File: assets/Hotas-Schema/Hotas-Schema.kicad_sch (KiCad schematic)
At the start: 22 parts, among them SW1 SW_SPST, SW10 SW_SPST, SW2 SW_SPST, SW3 SW_SPST, SW4 SW_SPST, SW5 SW_SPST, SW6 SW_SPST, SW7 SW_SPST, SW8 SW_SPST, SW9 SW_SPST

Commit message: Finish the circuit schematic
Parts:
- Joystick1: symbol IoT:Joystick -> HumanInterface:Joystick
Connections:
- net at ProMicro1.14 (GND): now also Joystick1. (Y)
- net at ProMicro1.16 (VCC): now also Joystick1. (Y), RV1.1
- net at ProMicro1.17 (A3): now also RV1.2
- net at ProMicro1.19 (A1): now also Joystick1. (Y)
- net at ProMicro1.20 (A0): now also Joystick1. (Y)
- net at ProMicro1.21 (15): now also Joystick1. (Y)
- net at ProMicro1.22 (14): now also SW10.1 (A)
- net at ProMicro1.4 (GND): now also RV1.3, SW10.2 (B)
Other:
- note added: "04-03-2024"
- note added: "1.0"
- note added: "Lego Throttle joystick schematic"
- moved on the sheet: Joystick1, RV1, SW10
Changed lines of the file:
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@@
   (junction (at 117.856 104.14) (diameter 0) (color 0 0 0 0)
   )
+  (junction (at 135.89 83.312) (diameter 0) (color 0 0 0 0)
+  )
   (junction (at 107.696 111.76) (diameter 0) (color 0 0 0 0)
   )
   (junction (at 131.826 91.44) (diameter 0) (color 0 0 0 0)
   )
+  (junction (at 135.89 44.704) (diameter 0) (color 0 0 0 0)
+  )
   (junction (at 121.666 99.06) (diameter 0) (color 0 0 0 0)
   )
@@
   (junction (at 121.666 124.46) (diameter 0) (color 0 0 0 0)
   )
+  (wire (pts (xy 129.794 62.992) (xy 132.08 62.992))
+    (stroke (width 0) (type default))
+  )
+  (wire (pts (xy 143.764 57.404) (xy 143.764 67.056))
+    (stroke (width 0) (type default))
+  )
   (wire (pts (xy 145.796 84.328) (xy 145.796 91.44))
     (stroke (width 0) (type default))
   )
+  (wire (pts (xy 129.794 73.152) (xy 140.208 73.152))
+    (stroke (width 0) (type default))
+  )
+  (wire (pts (xy 151.638 71.12) (xy 129.794 71.12))
+    (stroke (width 0) (type default))
+  )
+  (wire (pts (xy 135.89 44.704) (xy 138.43 44.704))
+    (stroke (width 0) (type default))
+  )
   (wire (pts (xy 106.426 69.088) (xy 103.886 69.088))
     (stroke (width 0) (type default))
@@
     (stroke (width 0) (type default))
   )
+  (wire (pts (xy 151.638 57.404) (xy 151.638 71.12))
+    (stroke (width 0) (type default))
+  )
   (wire (pts (xy 101.854 111.76) (xy 107.696 111.76))
     (stroke (width 0) (type default))
   )
+  (wire (pts (xy 135.89 44.704) (xy 135.89 55.118))
+    (stroke (width 0) (type default))
+  )
+  (wire (pts (xy 135.89 83.312) (xy 140.208 83.312))
+    (stroke (width 0) (type default))
+  )
   (wire (pts (xy 103.886 86.36) (xy 117.856 86.36))
     (stroke (width 0) (type default))
@@
     (stroke (width 0) (type default))
   )
+  (wire (pts (xy 119.126 46.736) (xy 138.43 46.736))
+    (stroke (width 0) (type default))
+  )
   (wire (pts (xy 104.902 71.12) (xy 106.426 71.12))
     (stroke (width 0) (type default))
@@
     (stroke (width 0) (type default))
   )
+  (wire (pts (xy 147.828 57.404) (xy 147.828 69.088))
+    (stroke (width 0) (type default))
+  )
   (wire (pts (xy 131.826 91.44) (xy 131.826 104.14))
     (stroke (width 0) (type default))
   )
+  (wire (pts (xy 143.764 67.056) (xy 129.794 67.056))
+    (stroke (width 0) (type default))
+  )
   (wire (pts (xy 145.796 104.14) (xy 145.796 116.84))
     (stroke (width 0) (type default))
@@
     (stroke (width 0) (type default))
   )
+  (wire (pts (xy 135.89 62.738) (xy 135.89 83.312))
+    (stroke (width 0) (type default))
+  )
   (wire (pts (xy 131.826 91.44) (xy 131.826 85.344))
     (stroke (width 0) (type default))
@@
     (stroke (width 0) (type default))
   )
+  (wire (pts (xy 147.828 69.088) (xy 129.794 69.088))
+    (stroke (width 0) (type default))
+  )
+  (wire (pts (xy 117.094 44.704) (xy 135.89 44.704))
+    (stroke (width 0) (type default))
+  )
+  (wire (pts (xy 119.126 83.312) (xy 135.89 83.312))
+    (stroke (width 0) (type default))
+  )
   (wire (pts (xy 117.856 86.36) (xy 117.856 91.44))
     (stroke (width 0) (type default))
   )
+  (wire (pts (xy 119.126 83.312) (xy 119.126 82.804))
+    (stroke (width 0) (type default))
+  )
   (wire (pts (xy 104.902 85.344) (xy 104.902 71.12))
     (stroke (width 0) (type default))
@@
     (stroke (width 0) (type default))
   )
+  (wire (pts (xy 117.094 46.736) (xy 117.094 44.704))
+    (stroke (width 0) (type default))
+  )
   (wire (pts (xy 131.826 104.14) (xy 131.826 116.84))
     (stroke (width 0) (type default))
@@
   (wire (pts (xy 101.854 65.024) (xy 101.854 111.76))
     (stroke (width 0) (type default))
+  )
+  (wire (pts (xy 132.08 62.992) (xy 132.08 58.928))
+    (stroke (width 0) (type default))
+  )
+  (text "1.0" (at 267.97 194.31 0)
+    (effects (font (size 1.27 1.27) (thickness 0.254) bold) (justify left bottom))
+  )
+  (text "Lego Throttle joystick schematic" (at 185.166 191.262 0)
+    (effects (font (size 2.54 2.54) (thickness 0.508) bold italic) (justify left bottom))
+  )
+  (text "04-03-2024" (at 205.74 194.31 0)
+    (effects (font (size 1.27 1.27)) (justify left bottom))
   )
   (symbol (lib_id "Switch:SW_SPST") (at 140.716 91.44 0) (unit 1)
@@
     )
   )
-  (symbol (lib_id "IoT:Joystick") (at 154.94 49.53 270) (unit 1)
-    (in_bom yes) (on_board yes) (dnp no) (fields_autoplaced)
-    (property "Reference" "Joystick1" (at 162.56 49.403 90)
-      (effects (font (size 1.27 1.27)) (justify left))
-    )
-    (property "Value" "~" (at 154.94 49.53 0)
-      (effects (font (size 1.27 1.27)))
-    )
-    (property "Footprint" "" (at 154.94 49.53 0)
-      (effects (font (size 1.27 1.27)) hide)
-    )
-    (property "Datasheet" "" (at 154.94 49.53 0)
+  (symbol (lib_id "HumanInterface:Joystick") (at 147.828 48.768 0) (unit 1)
+    (in_bom yes) (on_board yes) (dnp no) (fields_autoplaced)
+    (property "Reference" "Joystick1" (at 155.448 48.768 0)
+      (effects (font (size 1.27 1.27)) (justify left))
+    )
+    (property "Value" "~" (at 147.828 48.768 0)
+      (effects (font (size 1.27 1.27)))
+    )
+    (property "Footprint" "" (at 147.828 48.768 0)
+      (effects (font (size 1.27 1.27)) hide)
+    )
+    (property "Datasheet" "" (at 147.828 48.768 0)
       (effects (font (size 1.27 1.27)) hide)
     )
@@
     )
   )
-  (symbol (lib_id "Device:R_Potentiometer") (at 158.75 62.23 270) (unit 1)
-    (in_bom yes) (on_board yes) (dnp no) (fields_autoplaced)
-    (property "Reference" "RV1" (at 158.75 58.42 90)
-      (effects (font (size 1.27 1.27)))
-    )
-    (property "Value" "R_Potentiometer" (at 158.75 58.42 90)
-      (effects (font (size 1.27 1.27)) hide)
-    )
-    (property "Footprint" "" (at 158.75 62.23 0)
-      (effects (font (size 1.27 1.27)) hide)
-    )
-    (property "Datasheet" "~" (at 158.75 62.23 0)
+  (symbol (lib_id "Device:R_Potentiometer") (at 135.89 58.928 0) (mirror y) (unit 1)
+    (in_bom yes) (on_board yes) (dnp no)
+    (property "Reference" "RV1" (at 138.43 58.928 0)
+      (effects (font (size 1.27 1.27)) (justify right))
+    )
+    (property "Value" "R_Potentiometer" (at 139.7 58.928 90)
+      (effects (font (size 1.27 1.27)) hide)
+    )
+    (property "Footprint" "" (at 135.89 58.928 0)
+      (effects (font (size 1.27 1.27)) hide)
+    )
+    (property "Datasheet" "~" (at 135.89 58.928 0)
       (effects (font (size 1.27 1.27)) hide)
     )
@@
     )
   )
-  (symbol (lib_id "Switch:SW_SPST") (at 147.32 62.23 0) (unit 1)
-    (in_bom yes) (on_board yes) (dnp no) (fields_autoplaced)
-    (property "Reference" "SW10" (at 147.32 58.42 0)
-      (effects (font (size 1.27 1.27)))
-    )
-    (property "Value" "SW_SPST" (at 147.32 58.42 0)
-      (effects (font (size 1.27 1.27)) hide)
-    )
-    (property "Footprint" "" (at 147.32 62.23 0)
-      (effects (font (size 1.27 1.27)) hide)
-    )
-    (property "Datasheet" "~" (at 147.32 62.23 0)
-      (effects (font (size 1.27 1.27)) hide)
-    )
+  (symbol (lib_id "Switch:SW_SPST") (at 140.208 78.232 270) (unit 1)
+    (in_bom yes) (on_board yes) (dnp no) (fields_autoplaced)
+    (property "Reference" "SW10" (at 143.764 78.232 90)
+      (effects (font (size 1.27 1.27)) (justify left))
+    )
+    (property "Value" "SW_SPST" (at 144.018 78.232 0)
+      (effects (font (size 1.27 1.27)) hide)
+    )
+    (property "Footprint" "" (at 140.208 78.232 0)
+      (effects (font (size 1.27 1.27)) hide)
+    )
+    (property "Datasheet" "~" (at 140.208 78.232 0)
+      (effects (font (size 1.27 1.27)) hide)
+    )

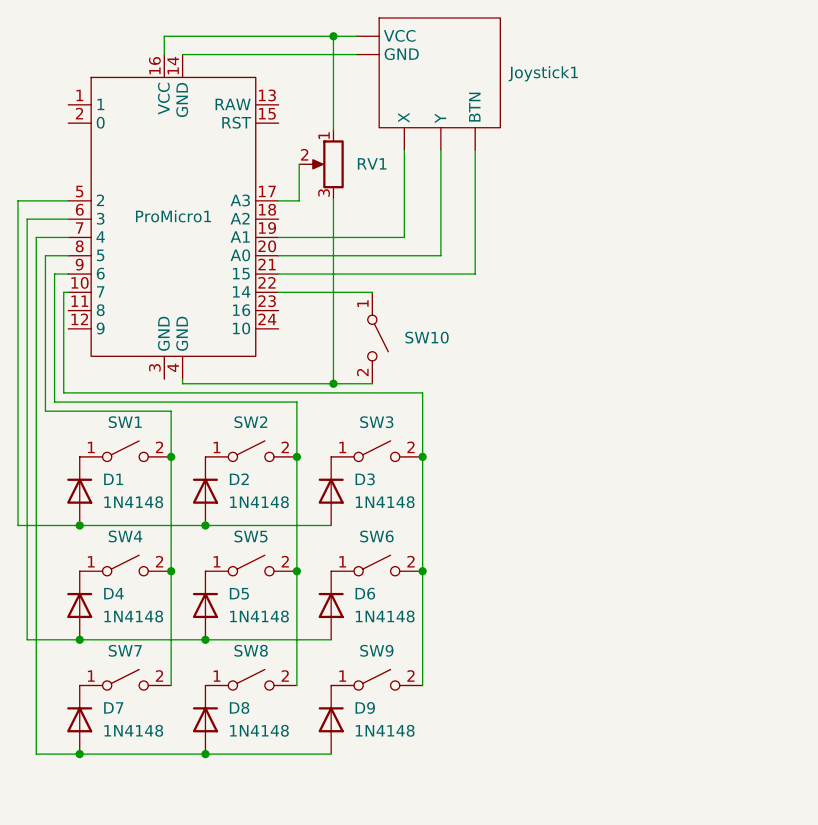
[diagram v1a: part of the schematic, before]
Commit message: Change labels in schematic
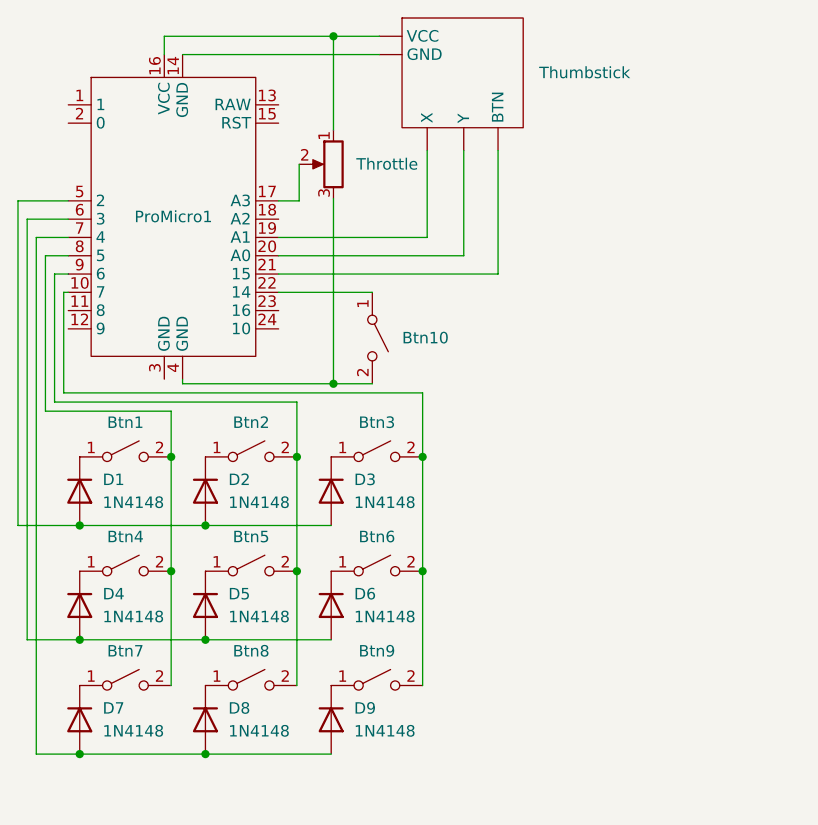
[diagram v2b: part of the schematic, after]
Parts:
- renumbered SW1 to Btn1, SW10 to Btn10, SW2 to Btn2, SW3 to Btn3, SW4 to Btn4, SW5 to Btn5, SW6 to Btn6, SW7 to Btn7, SW8 to Btn8, SW9 to Btn9, RV1 to Throttle, Joystick1 to Thumbstick
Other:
- moved on the sheet: Thumbstick
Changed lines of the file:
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@@
     (stroke (width 0) (type default))
   )
-  (wire (pts (xy 143.764 57.404) (xy 143.764 67.056))
+  (wire (pts (xy 146.304 57.404) (xy 146.304 67.056))
     (stroke (width 0) (type default))
   )
@@
     (stroke (width 0) (type default))
   )
-  (wire (pts (xy 151.638 71.12) (xy 129.794 71.12))
-    (stroke (width 0) (type default))
-  )
-  (wire (pts (xy 135.89 44.704) (xy 138.43 44.704))
+  (wire (pts (xy 117.094 44.704) (xy 135.89 44.704))
     (stroke (width 0) (type default))
   )
@@
     (stroke (width 0) (type default))
   )
-  (wire (pts (xy 151.638 57.404) (xy 151.638 71.12))
+  (wire (pts (xy 154.178 57.404) (xy 154.178 71.12))
     (stroke (width 0) (type default))
   )
@@
     (stroke (width 0) (type default))
   )
+  (wire (pts (xy 135.89 44.704) (xy 140.97 44.704))
+    (stroke (width 0) (type default))
+  )
   (wire (pts (xy 121.666 124.46) (xy 135.636 124.46))
     (stroke (width 0) (type default))
@@
     (stroke (width 0) (type default))
   )
-  (wire (pts (xy 119.126 46.736) (xy 138.43 46.736))
+  (wire (pts (xy 119.126 46.736) (xy 140.97 46.736))
     (stroke (width 0) (type default))
   )
@@
     (stroke (width 0) (type default))
   )
-  (wire (pts (xy 147.828 57.404) (xy 147.828 69.088))
+  (wire (pts (xy 150.368 57.404) (xy 150.368 69.088))
     (stroke (width 0) (type default))
   )
@@
     (stroke (width 0) (type default))
   )
-  (wire (pts (xy 143.764 67.056) (xy 129.794 67.056))
-    (stroke (width 0) (type default))
-  )
   (wire (pts (xy 145.796 104.14) (xy 145.796 116.84))
     (stroke (width 0) (type default))
@@
     (stroke (width 0) (type default))
   )
+  (wire (pts (xy 129.794 67.056) (xy 146.304 67.056))
+    (stroke (width 0) (type default))
+  )
   (wire (pts (xy 121.666 99.06) (xy 135.636 99.06))
     (stroke (width 0) (type default))
@@
     (stroke (width 0) (type default))
   )
+  (wire (pts (xy 129.794 71.12) (xy 154.178 71.12))
+    (stroke (width 0) (type default))
+  )
   (wire (pts (xy 131.826 91.44) (xy 131.826 85.344))
     (stroke (width 0) (type default))
@@
     (stroke (width 0) (type default))
   )
-  (wire (pts (xy 147.828 69.088) (xy 129.794 69.088))
-    (stroke (width 0) (type default))
-  )
-  (wire (pts (xy 117.094 44.704) (xy 135.89 44.704))
+  (wire (pts (xy 129.794 69.088) (xy 150.368 69.088))
     (stroke (width 0) (type default))
   )
@@
   (symbol (lib_id "Switch:SW_SPST") (at 140.716 91.44 0) (unit 1)
     (in_bom yes) (on_board yes) (dnp no)
-    (property "Reference" "SW3" (at 140.716 87.63 0)
+    (property "Reference" "Btn3" (at 140.716 87.63 0)
       (effects (font (size 1.27 1.27)))
     )
@@
       (project "Hotas-Schema"
         (path "/754fa901-14b3-4c66-8cc0-b832b5d65ab2"
-          (reference "SW3") (unit 1)
+          (reference "Btn3") (unit 1)
         )
       )
@@
   (symbol (lib_id "Switch:SW_SPST") (at 112.776 116.84 0) (unit 1)
     (in_bom yes) (on_board yes) (dnp no) (fields_autoplaced)
-    (property "Reference" "SW7" (at 112.776 113.03 0)
+    (property "Reference" "Btn7" (at 112.776 113.03 0)
       (effects (font (size 1.27 1.27)))
     )
@@
       (project "Hotas-Schema"
         (path "/754fa901-14b3-4c66-8cc0-b832b5d65ab2"
-          (reference "SW7") (unit 1)
+          (reference "Btn7") (unit 1)
         )
       )
@@
   (symbol (lib_id "Switch:SW_SPST") (at 112.776 104.14 0) (unit 1)
     (in_bom yes) (on_board yes) (dnp no)
-    (property "Reference" "SW4" (at 112.776 100.33 0)
+    (property "Reference" "Btn4" (at 112.776 100.33 0)
       (effects (font (size 1.27 1.27)))
     )
@@
       (project "Hotas-Schema"
         (path "/754fa901-14b3-4c66-8cc0-b832b5d65ab2"
-          (reference "SW4") (unit 1)
+          (reference "Btn4") (unit 1)
         )
       )
@@
   (symbol (lib_id "Switch:SW_SPST") (at 126.746 104.14 0) (unit 1)
     (in_bom yes) (on_board yes) (dnp no)
-    (property "Reference" "SW5" (at 126.746 100.33 0)
+    (property "Reference" "Btn5" (at 126.746 100.33 0)
       (effects (font (size 1.27 1.27)))
     )
@@
       (project "Hotas-Schema"
         (path "/754fa901-14b3-4c66-8cc0-b832b5d65ab2"
-          (reference "SW5") (unit 1)
+          (reference "Btn5") (unit 1)
         )
       )
@@
     )
   )
-  (symbol (lib_id "HumanInterface:Joystick") (at 147.828 48.768 0) (unit 1)
-    (in_bom yes) (on_board yes) (dnp no) (fields_autoplaced)
-    (property "Reference" "Joystick1" (at 155.448 48.768 0)
-      (effects (font (size 1.27 1.27)) (justify left))
-    )
-    (property "Value" "~" (at 147.828 48.768 0)
-      (effects (font (size 1.27 1.27)))
-    )
-    (property "Footprint" "" (at 147.828 48.768 0)
-      (effects (font (size 1.27 1.27)) hide)
-    )
-    (property "Datasheet" "" (at 147.828 48.768 0)
+  (symbol (lib_id "HumanInterface:Joystick") (at 150.368 48.768 0) (unit 1)
+    (in_bom yes) (on_board yes) (dnp no) (fields_autoplaced)
+    (property "Reference" "Thumbstick" (at 158.75 48.768 0)
+      (effects (font (size 1.27 1.27)) (justify left))
+    )
+    (property "Value" "~" (at 150.368 48.768 0)
+      (effects (font (size 1.27 1.27)))
+    )
+    (property "Footprint" "" (at 150.368 48.768 0)
+      (effects (font (size 1.27 1.27)) hide)
+    )
+    (property "Datasheet" "" (at 150.368 48.768 0)
       (effects (font (size 1.27 1.27)) hide)
     )
@@
       (project "Hotas-Schema"
         (path "/754fa901-14b3-4c66-8cc0-b832b5d65ab2"
-          (reference "Joystick1") (unit 1)
+          (reference "Thumbstick") (unit 1)
         )
       )
@@
   (symbol (lib_id "Switch:SW_SPST") (at 112.776 91.44 0) (unit 1)
     (in_bom yes) (on_board yes) (dnp no)
-    (property "Reference" "SW1" (at 112.776 87.63 0)
+    (property "Reference" "Btn1" (at 112.776 87.63 0)
       (effects (font (size 1.27 1.27)))
     )
@@
       (project "Hotas-Schema"
         (path "/754fa901-14b3-4c66-8cc0-b832b5d65ab2"
-          (reference "SW1") (unit 1)
+          (reference "Btn1") (unit 1)
         )
       )
@@
   (symbol (lib_id "Switch:SW_SPST") (at 126.746 91.44 0) (unit 1)
     (in_bom yes) (on_board yes) (dnp no)
-    (property "Reference" "SW2" (at 126.746 87.63 0)
+    (property "Reference" "Btn2" (at 126.746 87.63 0)
       (effects (font (size 1.27 1.27)))
     )
@@
       (project "Hotas-Schema"
         (path "/754fa901-14b3-4c66-8cc0-b832b5d65ab2"
-          (reference "SW2") (unit 1)
+          (reference "Btn2") (unit 1)
         )
       )
@@
   (symbol (lib_id "Device:R_Potentiometer") (at 135.89 58.928 0) (mirror y) (unit 1)
     (in_bom yes) (on_board yes) (dnp no)
-    (property "Reference" "RV1" (at 138.43 58.928 0)
+    (property "Reference" "Throttle" (at 138.43 58.928 0)
       (effects (font (size 1.27 1.27)) (justify right))
     )
@@
       (project "Hotas-Schema"
         (path "/754fa901-14b3-4c66-8cc0-b832b5d65ab2"
-          (reference "RV1") (unit 1)
+          (reference "Throttle") (unit 1)
         )
       )
@@
   (symbol (lib_id "Switch:SW_SPST") (at 140.208 78.232 270) (unit 1)
     (in_bom yes) (on_board yes) (dnp no) (fields_autoplaced)
-    (property "Reference" "SW10" (at 143.764 78.232 90)
+    (property "Reference" "Btn10" (at 143.51 78.232 90)
       (effects (font (size 1.27 1.27)) (justify left))
     )
@@
       (project "Hotas-Schema"
         (path "/754fa901-14b3-4c66-8cc0-b832b5d65ab2"
-          (reference "SW10") (unit 1)
+          (reference "Btn10") (unit 1)
         )
       )
@@
   (symbol (lib_id "Switch:SW_SPST") (at 140.716 116.84 0) (unit 1)
     (in_bom yes) (on_board yes) (dnp no) (fields_autoplaced)
-    (property "Reference" "SW9" (at 140.716 113.03 0)
+    (property "Reference" "Btn9" (at 140.716 113.03 0)
       (effects (font (size 1.27 1.27)))
     )
@@
       (project "Hotas-Schema"
         (path "/754fa901-14b3-4c66-8cc0-b832b5d65ab2"
-          (reference "SW9") (unit 1)
+          (reference "Btn9") (unit 1)
         )
       )
@@
   (symbol (lib_id "Switch:SW_SPST") (at 140.716 104.14 0) (unit 1)
     (in_bom yes) (on_board yes) (dnp no)
-    (property "Reference" "SW6" (at 140.716 100.33 0)
+    (property "Reference" "Btn6" (at 140.716 100.33 0)
       (effects (font (size 1.27 1.27)))
     )
@@
       (project "Hotas-Schema"
         (path "/754fa901-14b3-4c66-8cc0-b832b5d65ab2"
-          (reference "SW6") (unit 1)
+          (reference "Btn6") (unit 1)
         )
       )
@@
   (symbol (lib_id "Switch:SW_SPST") (at 126.746 116.84 0) (unit 1)
     (in_bom yes) (on_board yes) (dnp no) (fields_autoplaced)
-    (property "Reference" "SW8" (at 126.746 113.03 0)
+    (property "Reference" "Btn8" (at 126.746 113.03 0)
       (effects (font (size 1.27 1.27)))
     )
@@
       (project "Hotas-Schema"
         (path "/754fa901-14b3-4c66-8cc0-b832b5d65ab2"
-          (reference "SW8") (unit 1)
-        )
-      )
+          (reference "Btn8") (unit 1)
+        )
+      )
